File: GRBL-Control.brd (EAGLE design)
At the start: 100 x 100 mm, 55 parts, among them IC3 4050D, IC4 LP298XS, J1 MICRO SD, SW1 B3U-1000PM-B, SW2 B3U-1000PM-B, SW3 B3U-1000PM-B, SW4 B3U-1000PM-B, U1 ARDUINO, U2 ARDUINO MICRO, U3 LM2596, X1 MSTBA2, X2 MSTBA8, X3 MSTBA12

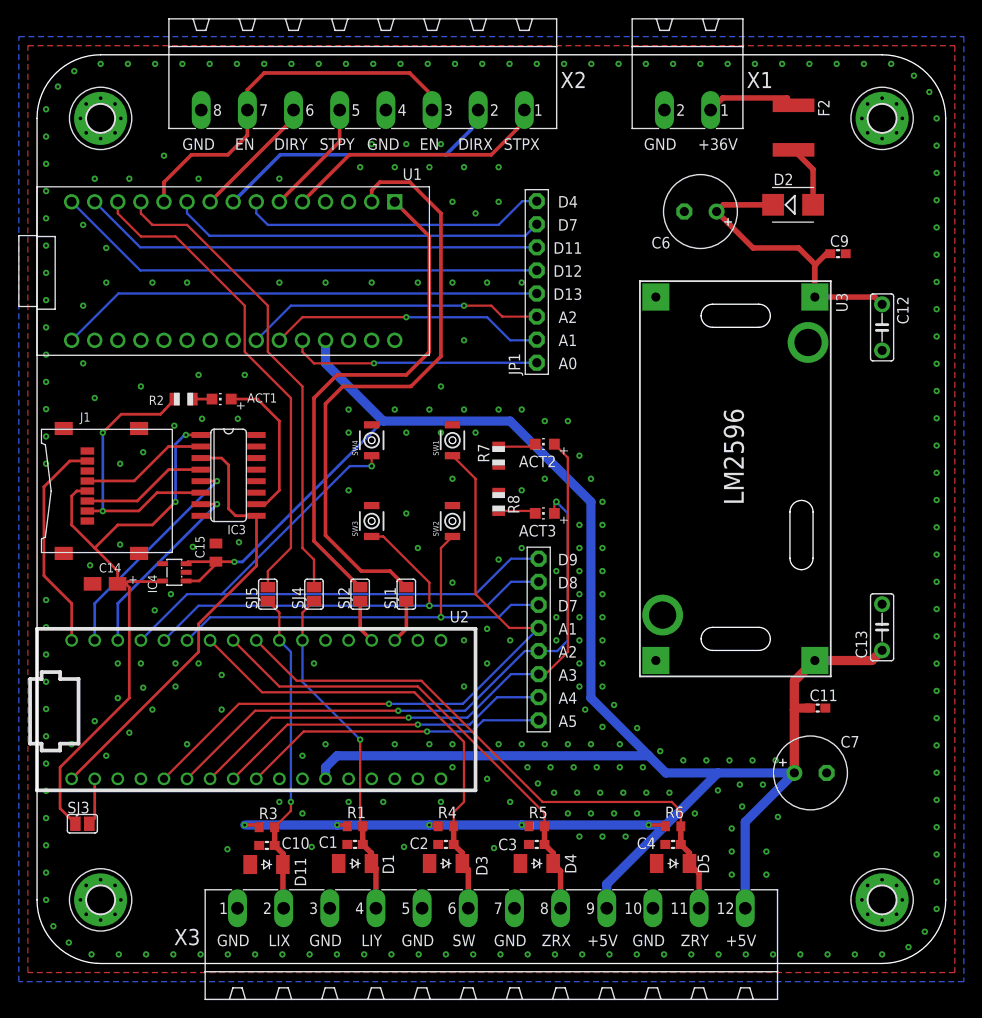
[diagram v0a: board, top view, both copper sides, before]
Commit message: v1.1 changed level converter for SD card, added soldering place and some other minor changes
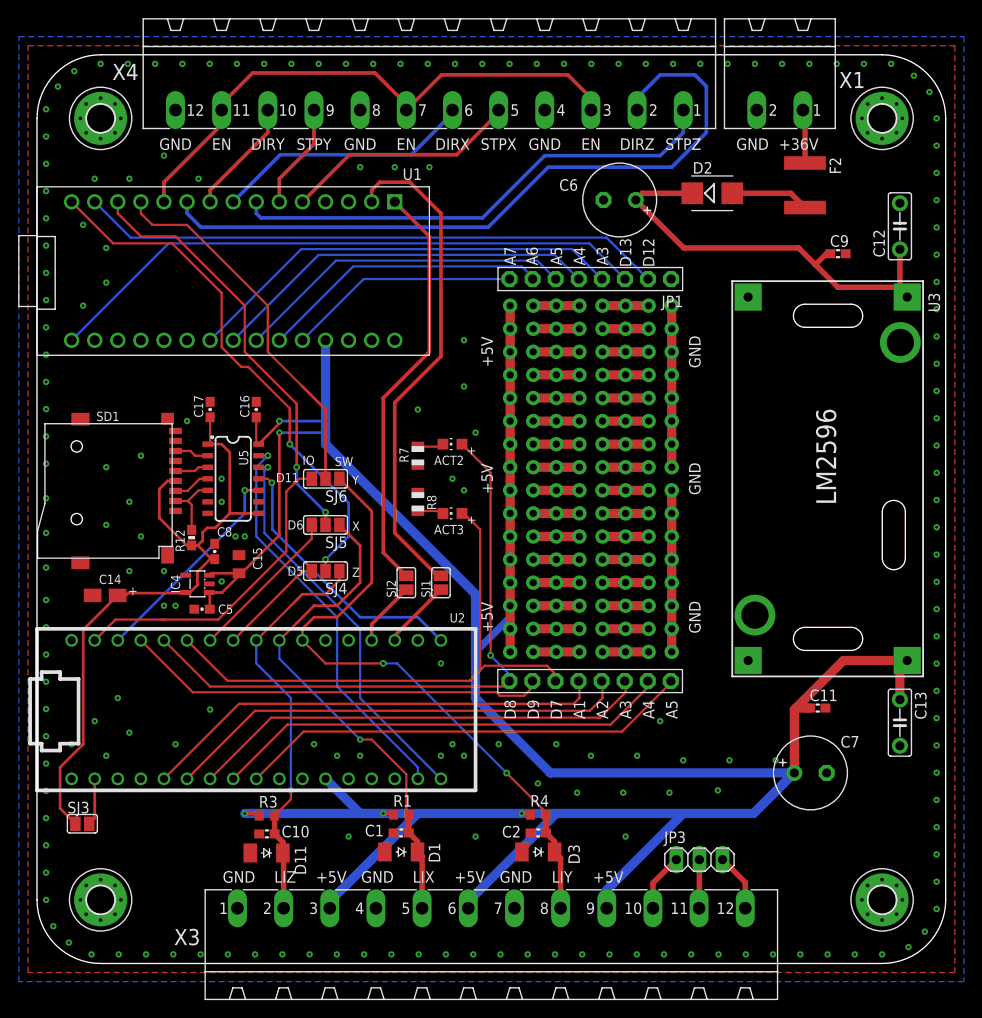
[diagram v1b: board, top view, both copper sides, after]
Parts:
- removed ACT1: RED, adafruit:CHIP-LED0805
- removed C3, C4: 100n, Parts:C0603
- removed D4, D5: CGRM4001-G, Parts:SOD-123_MINI-SMA
- removed IC3: 4050D, 40xx:SO16
- removed J1: MICRO SD, sd-mmc:TRANSFLASH-LOCK-SOCK
- removed R2: 1K, adafruit:R0805
- removed R5, R6: (no value), Parts:R0603
- removed SW1, SW2, SW3, SW4: B3U-1000PM-B, Parts:OMRON
- removed X2: MSTBA8, Parts:MSTBA8
- added C16, C17: 0.1uF, SparkFun-Capacitors:0603-CAP
- added C5, C8: 1.0uF, SparkFun-Capacitors:0603-CAP
- added JP3: (no value), pinhead:1X03
- added R12: 100k, SparkFun-Resistors:0603-RES
- added SD1: TF-HOLDER, sd-mmc:TF-PULL
- added SJ6: (no value), jumper:SJ_2
- added U$1, U$2: DEV_GRID, Components:DEV_GRID
- added U5: TXB0104, SparkFun-DigitalIC:SO14
- added X4: MSTBA12, con-phoenix-508:MSTBA12
- SJ4, SJ5: device jumper:SJ -> jumper:SJ_2
- moved C12 11.3 mm to (95.0, 81.1), turned to 90 degrees
- moved C13 10.7 mm to (95.0, 26.5), turned to 270 degrees
- moved C2 10.2 mm to (55.2, 14.4)
- moved D3 10.2 mm to (55.2, 12.3)
- moved R4 10.2 mm to (55.2, 16.4)
- moved U3 10.2 mm to (76.5, 75.1)
- moved ACT2 10.2 mm to (45.7, 57.1)
- moved ACT3 10.2 mm to (45.7, 49.5)
- moved X1 10.2 mm to (81.8, 99.0)
- moved SJ5 9.92 mm to (31.8, 48.3), turned to 180 degrees
- moved D2 8.98 mm to (74.3, 84.8)
- moved C6 8.98 mm to (64.1, 84.0)
- moved R7 8.89 mm to (41.9, 55.9)
- moved R8 8.89 mm to (41.9, 50.8)
- moved JP2 7.27 mm to (60.9, 31.1), turned to 180 degrees
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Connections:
- removed net NA0: JP1.1, U1.26
- removed net NA1: JP1.2, U1.25
- removed net NA2: JP1.3, U1.24
- removed net ND11: JP1.6, U1.14
- removed net ND12: JP1.5, U1.15
- removed net ND13: JP1.4, U1.16
- removed net ND4: JP1.8, U1.7
- removed net ND7: JP1.7, U1.10
- removed net USERSW: C2.1, D3.C, R4.2, U2.D6, X3.6
- removed net ZEROX: C3.1, D4.C, R5.2, U2.D5, X3.8
- removed net ZEROY: C4.1, D5.C, R6.2, U2.D4, X3.11
- new net !CS_3V3: R12.1, SD1.2, U5.5
- new net CLK_3V3: SD1.5, U5.3
- new net D11: SJ6.3, U2.D11
- new net D12: U2.D12
- new net D5: SJ4.3, U2.D5
- new net D6: SJ5.3, U2.D6
- new net DI_3V3: SD1.3, U5.4
- new net DO_3V3: SD1.7, U5.2
- new net LIMITZ: C10.1, D11.C, R3.2, SJ4.1, U2.D4, X3.2
- new net N$14: JP3.2, X3.11
- new net N$15: JP3.3, X3.12
- new net N$4: U1.7, X4.1
- new net N$5: U1.10, X4.2
- new net N$6: JP1.8, U1.26
- new net N$7: JP1.7, U1.25
- new net N$8: JP1.6, U1.24
- new net NLIMITZ: SJ4.2, U1.15
- net +3V3: now also C17.1, C8.2, R12.2, SD1.4, U5.1, U5.8; no longer IC3.1, J1.4
- net +5V: now also C16.1, C5.1, U$1.+, U$1.P$49, U$1.P$50, U$1.P$51, U$1.P$52, U$1.P$53, U$1.P$54, U$1.P$55, U$2.+, U$2.P$49, U$2.P$50, U$2.P$51, U$2.P$52, U$2.P$53, U$2.P$54, U$2.P$55, U5.14, X3.3, X3.6; no longer R5.1, R6.1, X3.12
- net A1: no longer SW1.P$1
- net A2: no longer ACT3.A
- net A3: no longer ACT2.A
- net CLK: now also U2.SCK, U5.12; no longer IC3.3, IC3.9, U2.D13
- net CS: now also U5.10; no longer IC3.7
- net D7: now also ACT3.A; no longer SW2.P$1
- net D8: now also ACT2.A, JP2.8; no longer JP2.7, SW3.P$1
- net D9: now also JP2.7; no longer JP2.8, SW4.P$1
- net DI: now also U2.MOSI, U5.11; no longer IC3.5, U2.D11
- net DIRX: now also X4.6; no longer X2.2
- net DIRY: now also X4.10; no longer X2.6
- net DO: now also U2.MISO, U5.13; no longer J1.7, U2.D12
- net GND: now also C16.2, C17.2, C5.2, C8.1, SD1.6, SD1.S1, SD1.S2, SD1.S3, SD1.S4, U$1.-, U$1.P$57, U$1.P$58, U$1.P$59, U$1.P$60, U$1.P$61, U$1.P$62, U$1.P$63, U$2.-, U$2.P$57, U$2.P$58, U$2.P$59, U$2.P$60, U$2.P$61, U$2.P$62, U$2.P$63, U5.7, X3.4, X4.12, X4.4, X4.8; no longer C3.2, C4.2, D4.A, D5.A, IC3.11, IC3.14, IC3.8, J1.6, J1.S1, J1.S2, J1.S3, J1.S4, SW1.P$2, SW2.P$2, SW3.P$2, SW4.P$2, X2.4, X2.8, X3.10, X3.3, X3.5
- net LIMITX: now also C1.1, D1.C, R1.2, U2.D3, X3.5; no longer U1.13
- net LIMITY: now also C2.1, D3.C, R4.2, SJ6.1, U2.D2, X3.8; no longer SJ4.1, U1.12
- net N$10: now also JP1.4, U1.22; no longer IC3.2, J1.5
- net N$11: now also JP1.3, U1.16; no longer IC3.6, J1.2, R2.1
- net N$12: now also JP1.2, U1.14; no longer ACT1.C, R2.2
- net N$13: now also JP3.1, X3.10; no longer IC3.4, J1.3
- net N$9: now also JP1.5, U1.23; no longer ACT1.A, IC3.10
- net NLIMITX: now also U1.13; no longer C10.1, D11.C, R3.2, U2.D3, X3.2
- net NLIMITY: now also SJ6.2, U1.12; no longer C1.1, D1.C, R1.2, SJ4.2, U2.D2, X3.4
- net STEP-EN: now also X4.11, X4.3, X4.7; no longer X2.3, X2.7
- net STEPX: now also X4.5; no longer X2.1
- net STEPY: now also X4.9; no longer X2.5
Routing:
- net N$5: track 0.00 -> 79.0 mm
- net ZEROY: track 66.0 -> 0.00 mm
- net N$12: track 2.14 -> 64.4 mm
- net NLIMITZ: track 0.00 -> 58.6 mm, vias 0 -> 2
- net N$4: track 0.00 -> 54.8 mm
- net ND12: track 54.3 -> 0.00 mm
- net ZEROX: track 53.3 -> 0.00 mm
- net ND13: track 53.3 -> 0.00 mm
- net USERSW: track 52.0 -> 0.00 mm
- net ND11: track 50.7 -> 0.00 mm
- net LIMITZ: track 0.00 -> 45.1 mm, vias 0 -> 1
- net ND7: track 41.3 -> 0.00 mm
- net N$8: track 0.00 -> 37.4 mm
- net N$11: track 31.8 -> 66.9 mm, vias 2 -> 0
- net D11: track 0.00 -> 35.1 mm
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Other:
- board text added: "A6"
- board text added: "A7"
- board text added: "D5"
- board text added: "D6"
- board text added: "DIRZ"
- board text added: "GRBL Controller v1.1"
- board text added: "IO"
- board text added: "LIZ"
- board text added: "Mid 2020"
- board text added: "STPZ"
- board text added: "X"
- board text added: "Y"
- board text added: "Z"
- board text added: "andrejspukitis.lv"
- board text added: "edgars.dev"
- board text removed: "A0"
- board text removed: "D4"
- board text removed: "ZRX"
- board text removed: "ZRY"
